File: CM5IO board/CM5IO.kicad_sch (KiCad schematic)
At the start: 14 parts, among them J10 USB_C_Receptacle_USB2.0, J11 USB_C_Receptacle_USB2.0

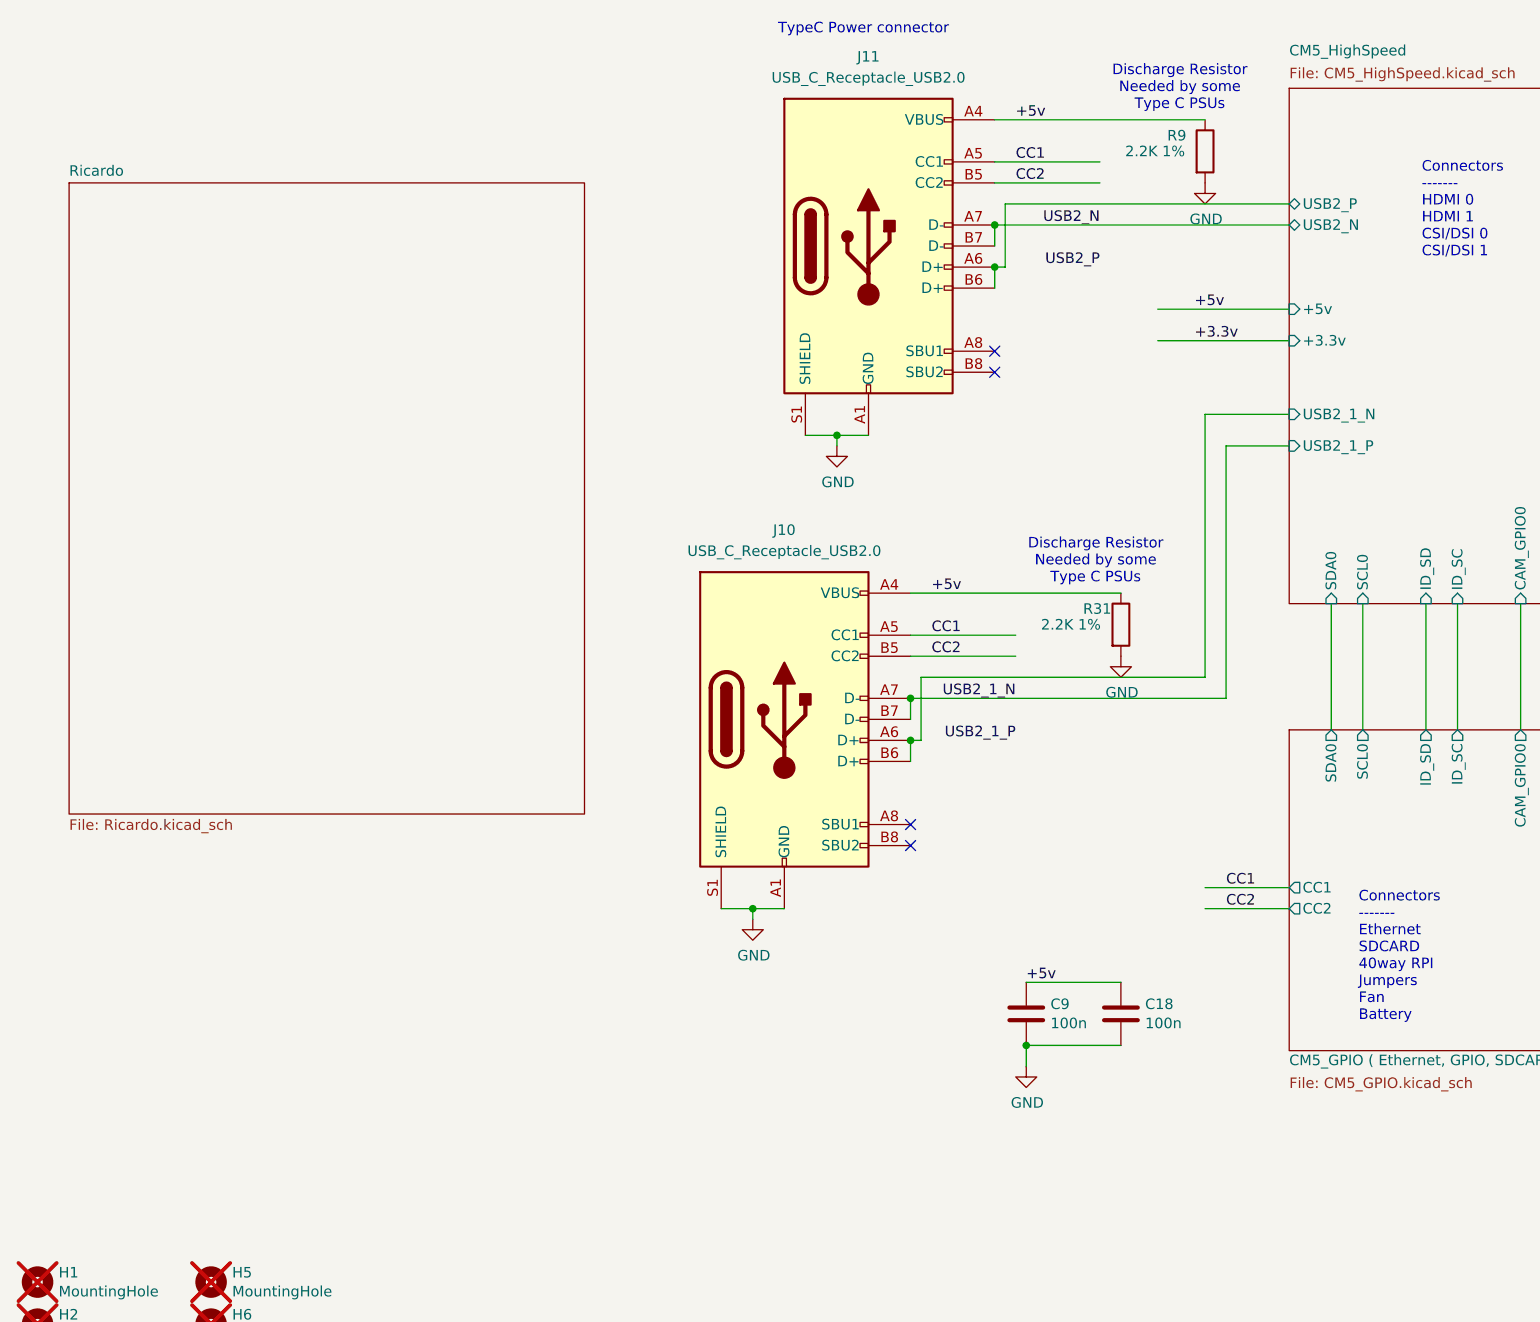
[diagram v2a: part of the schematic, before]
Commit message: Added "Buck Boost" hierarchical sheet; Deleted two USB-C ports
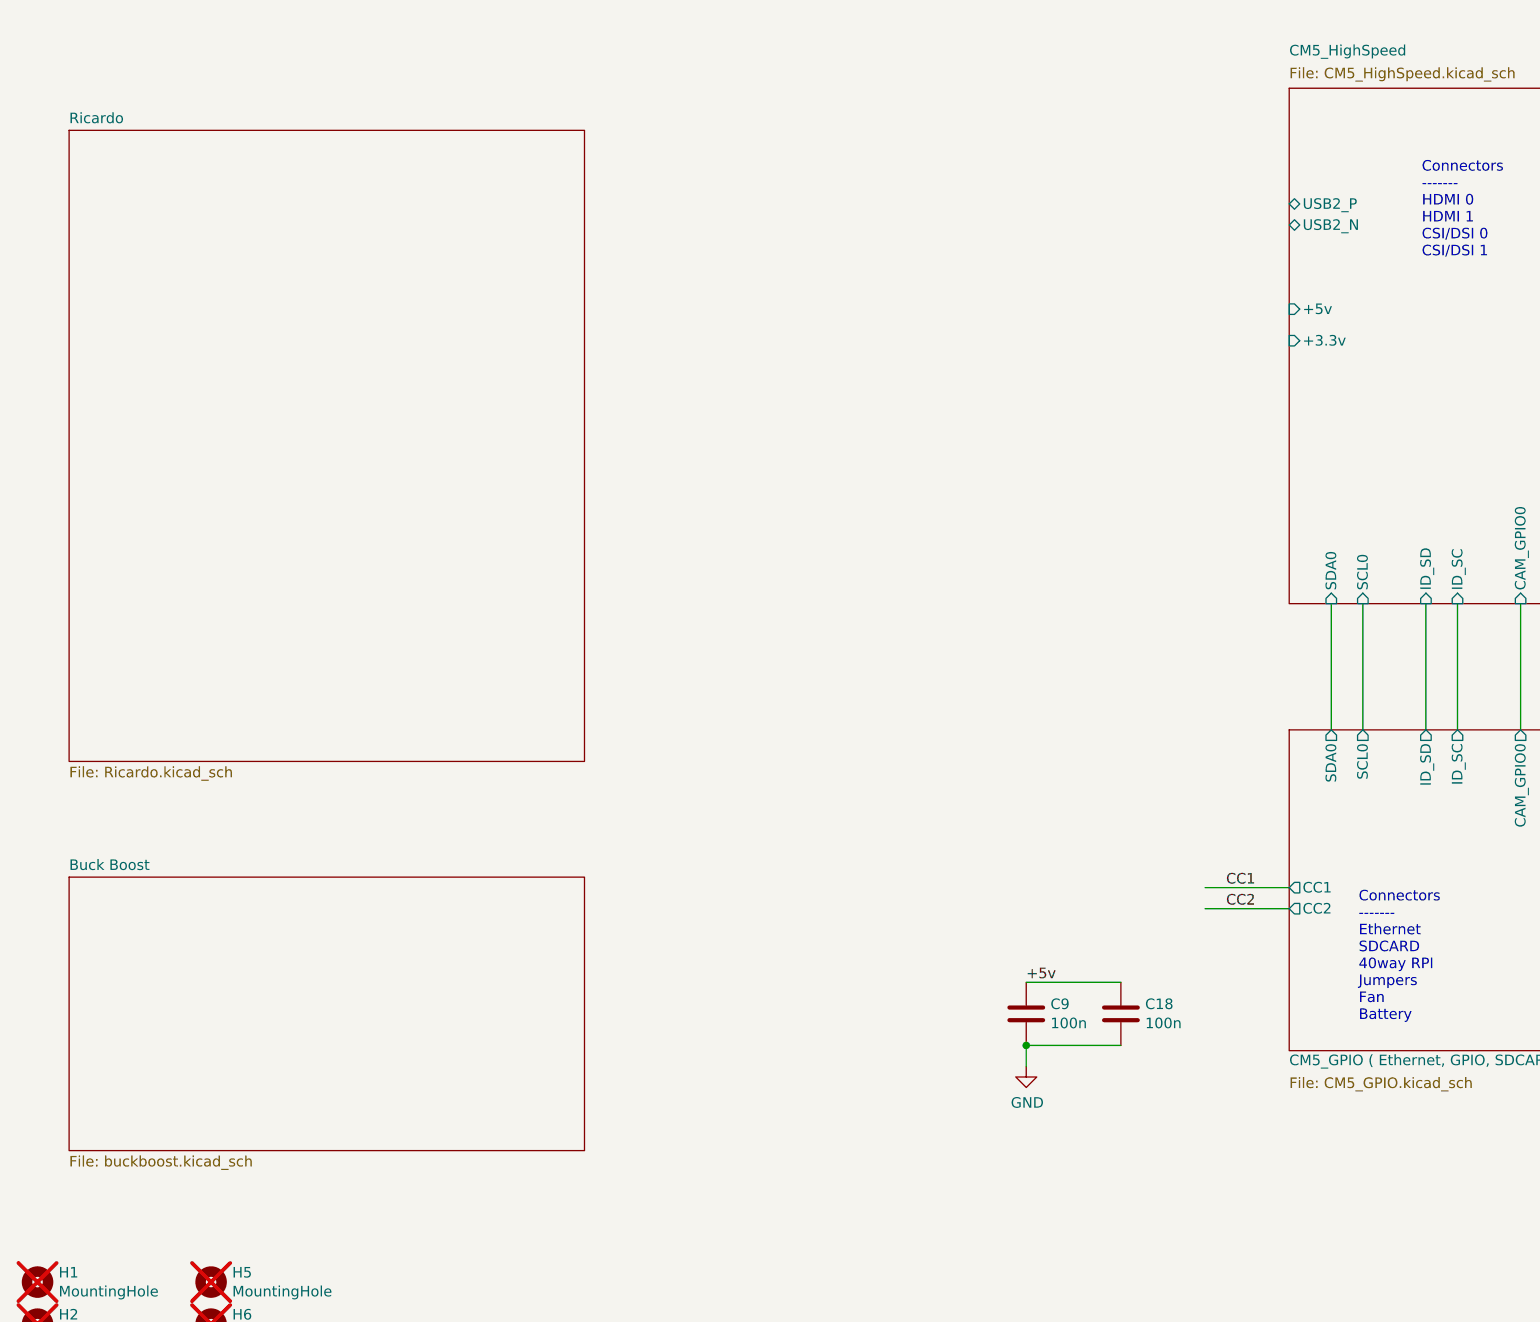
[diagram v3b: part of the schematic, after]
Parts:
- removed J10, J11: USB_C_Receptacle_USB2.0, Connector_USB:USB_C_Receptacle_GCT_USB4105-xx-A_16P_TopMnt_Horizontal, symbol Connector:USB_C_Receptacle_USB2.0_16P
- removed R31, R9: 2.2K 1%, Resistor_SMD:R_0402_1005Metric, symbol Device:R
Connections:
- no-connect marks 4 -> 0
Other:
- added sheet Buck Boost (buckboost.kicad_sch)
- sheet CM5_HighSpeed ports: added none; removed USB2_1_N, USB2_1_P
- note removed: "Discharge Resistor Needed by some Type C PSUs"
- note removed: "TypeC Power connector"
